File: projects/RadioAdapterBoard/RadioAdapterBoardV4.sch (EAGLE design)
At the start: 33 parts

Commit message: Radio Adapter Board PCB Ready
Also, minor edits to 0805 package, L3255M package, and job
sfe-ger274x.cam
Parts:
- C14, C15, C16, C17, C18, C19, C20, C21, C22, C23: device CNTRL_BOARD:CAP0805 -> BrownSpaceEngineering:CAP0805
- R10, R11, R12, R5, R6, R7, R8, R9: device CNTRL_BOARD:RESISTOR -> BrownSpaceEngineering:RES0805
- renumbered PWR_ON to PWR
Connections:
- net 3V6: now also C19.P$1, C23.P$1; no longer C19.1, C23.1
- net 3V6-SNS: now also C18.P$1; no longer C18.1
- net COMP: now also C14.P$2, C15.P$1; no longer C14.2, C15.1
- net FB: now also C15.P$2; no longer C15.2
- net GND: now also C16.P$2, C17.P$2, C18.P$2, C19.P$2, C20.P$1; no longer C16.2, C17.2, C18.2, C19.2, C20.1
- net N$23: now also C20.P$2; no longer C20.2
- net N$25: now also C22.P$1; no longer C22.1
- net N$26: now also C22.P$2; no longer C22.2
- net N$28: now also C21.P$2; no longer C21.2
- net N$29: now also C21.P$1; no longer C21.1
- net N$4: now also C14.P$1; no longer C14.1
- net N$5: now also C23.P$2; no longer C23.2
- net OVP: now also C17.P$1; no longer C17.1
- net VIN: now also C16.P$1; no longer C16.1

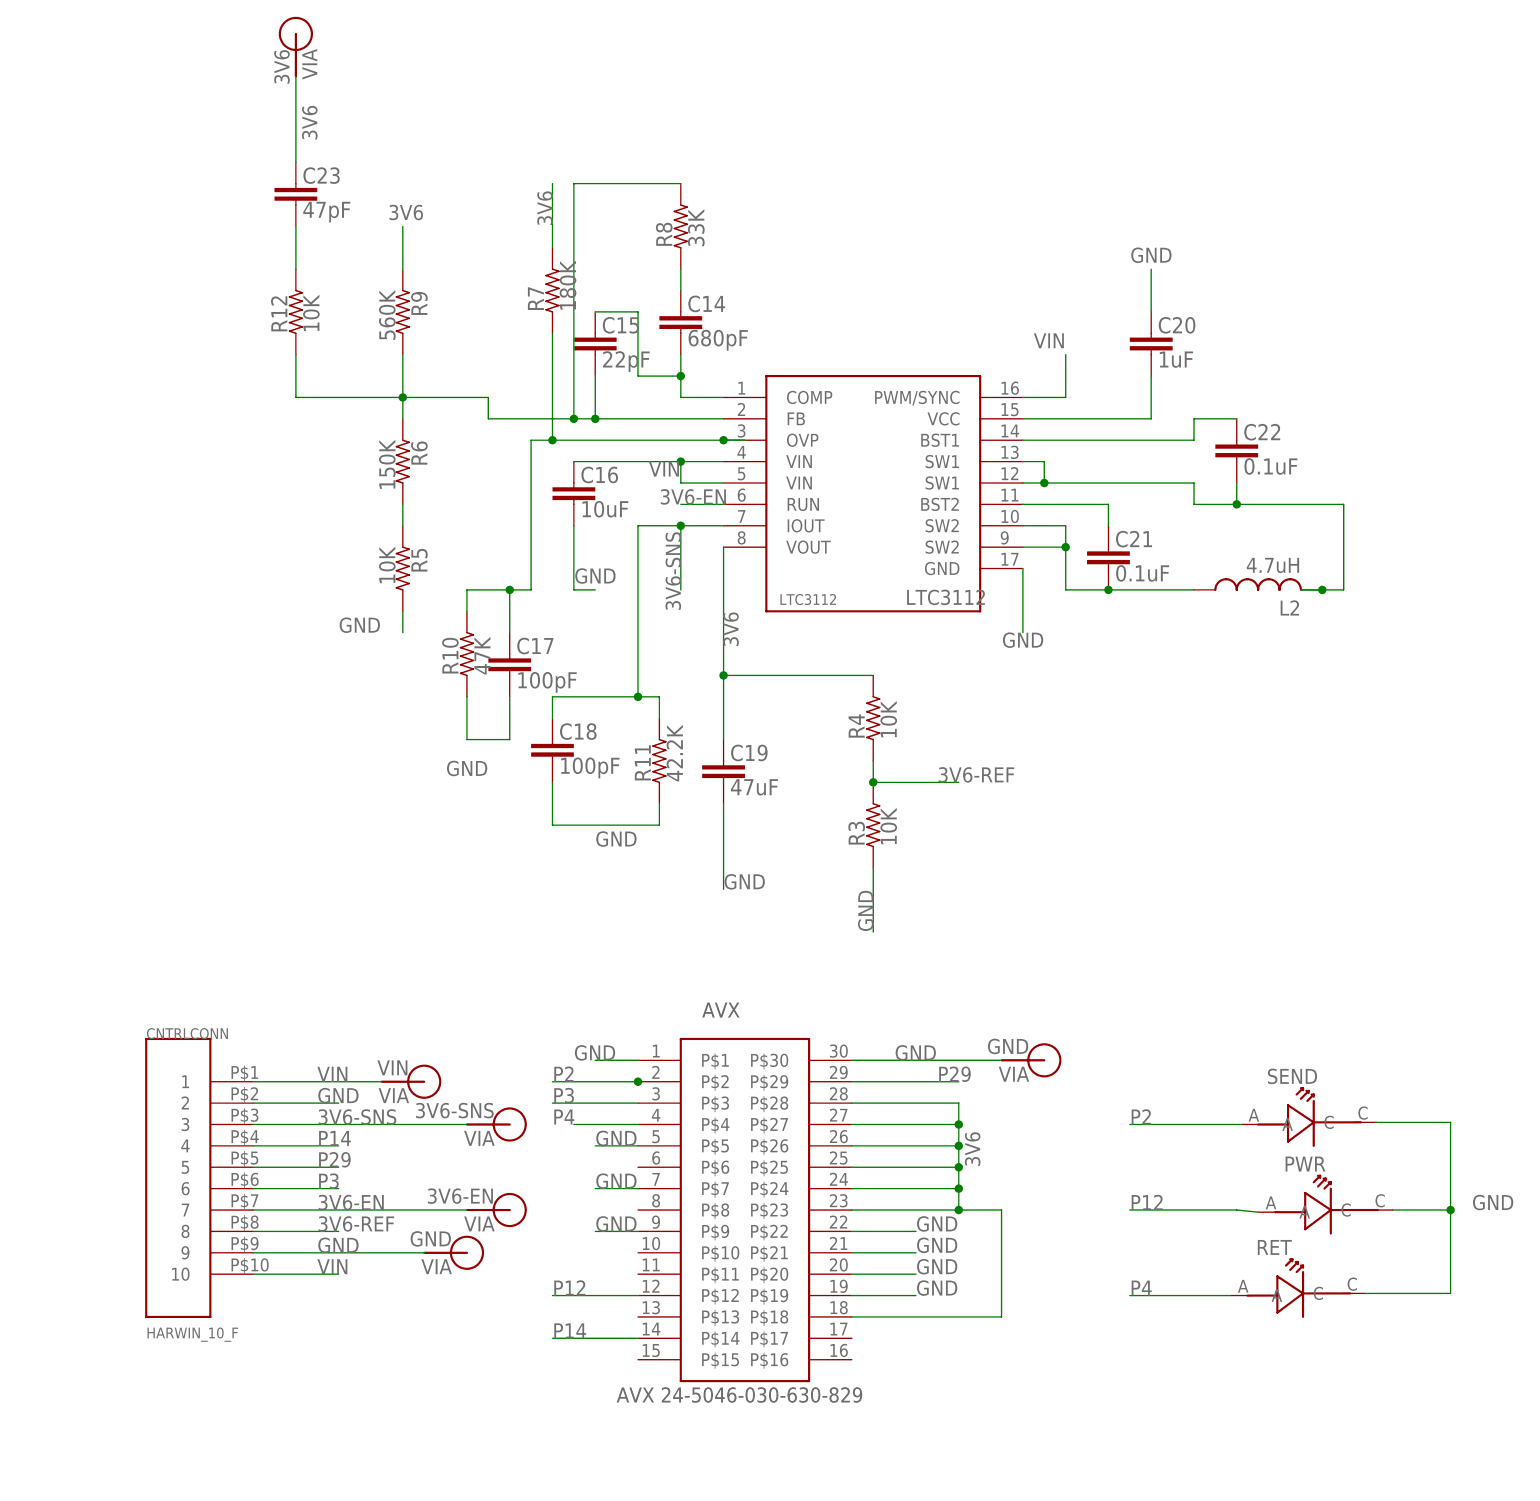
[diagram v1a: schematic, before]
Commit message: Updates to Radio Adapter Board, Driver Board, Flash Panel. Somebody forgot to commit for a whole week or so....
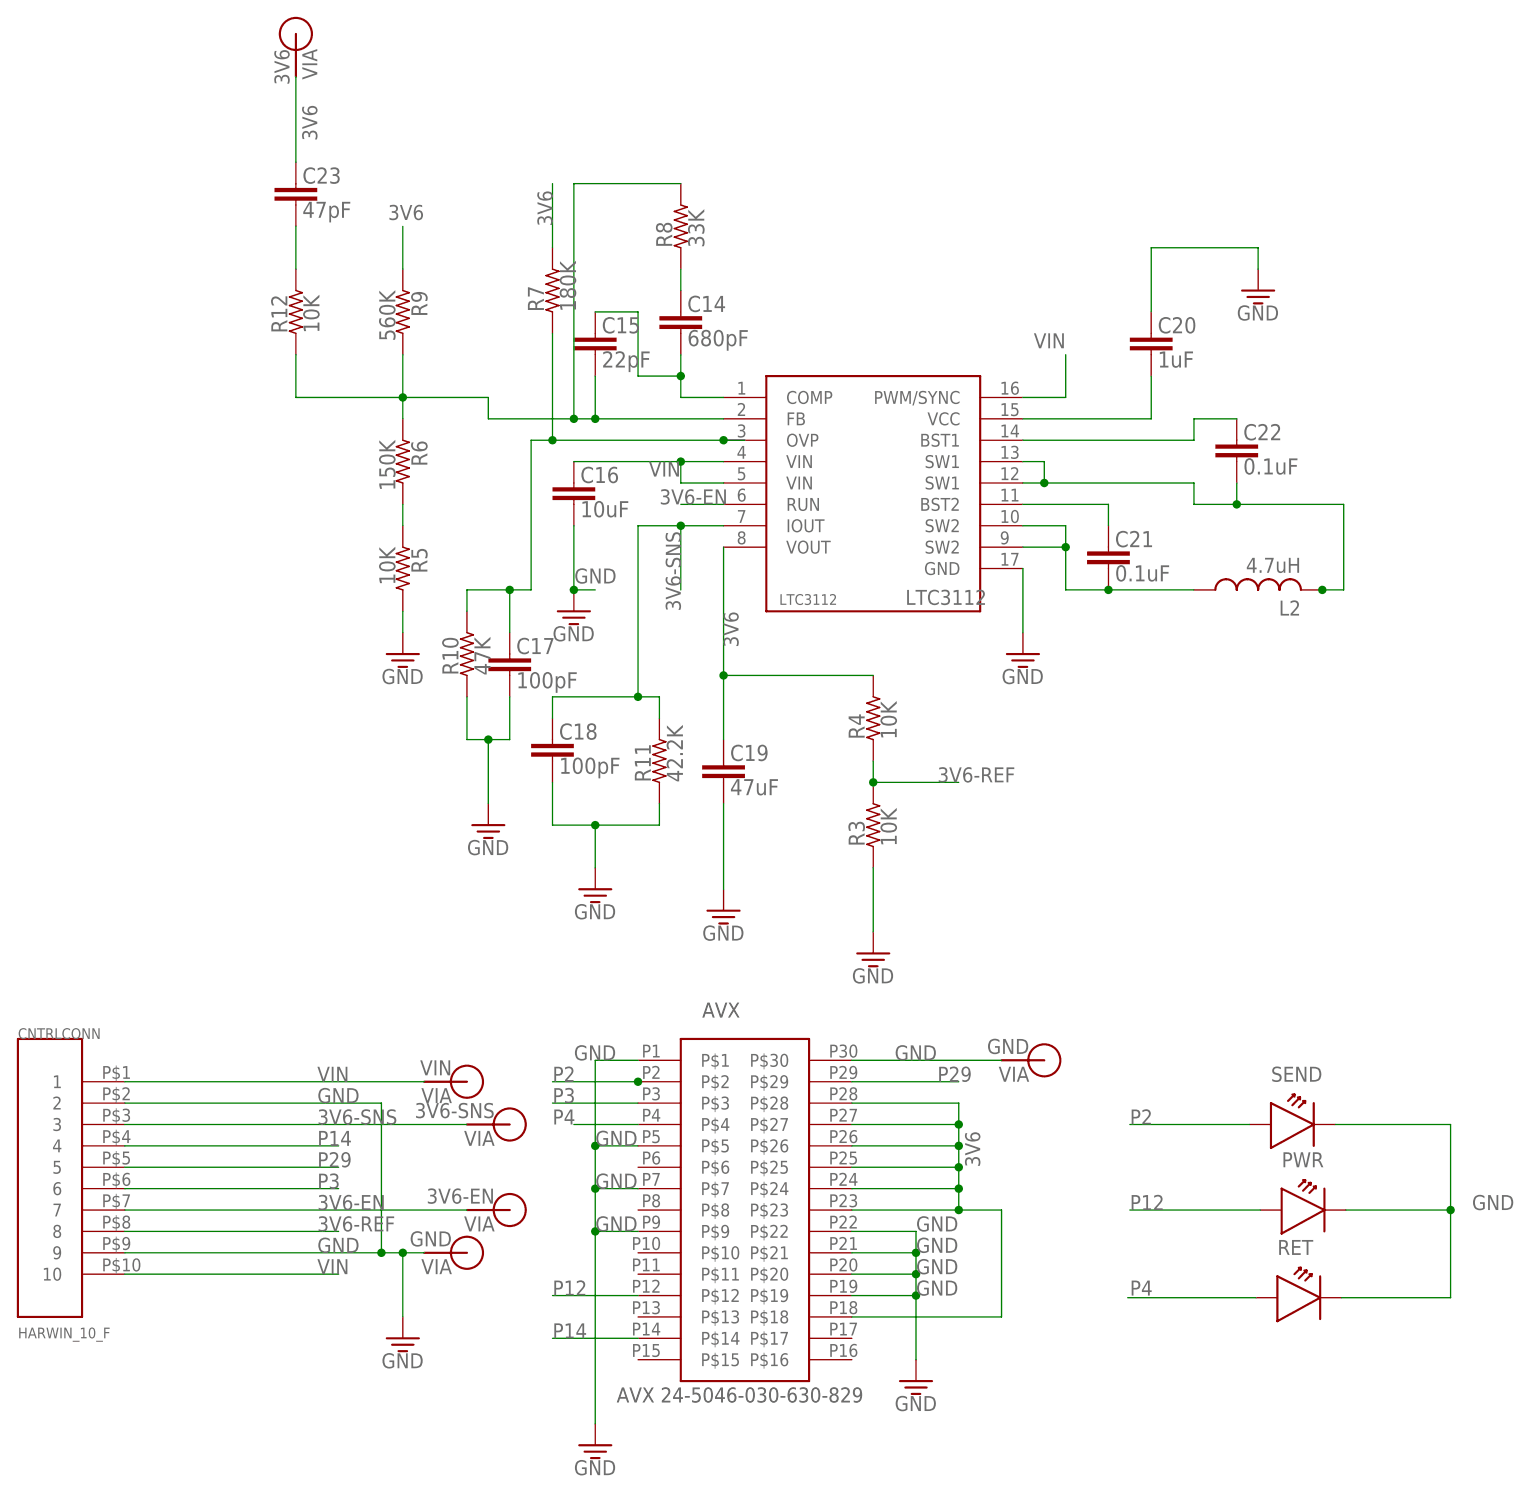
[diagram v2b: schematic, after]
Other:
- moved on the sheet: CNTRLCONN
